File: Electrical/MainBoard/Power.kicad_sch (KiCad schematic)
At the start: 17 parts, among them J13 USB_B_Micro, J14 Battery1, J2 3.3V Supply, J3 5V Supply, SW1 5V Bypass, SW2 All Power Switch, U1 AP2114HA-3.3TRG1

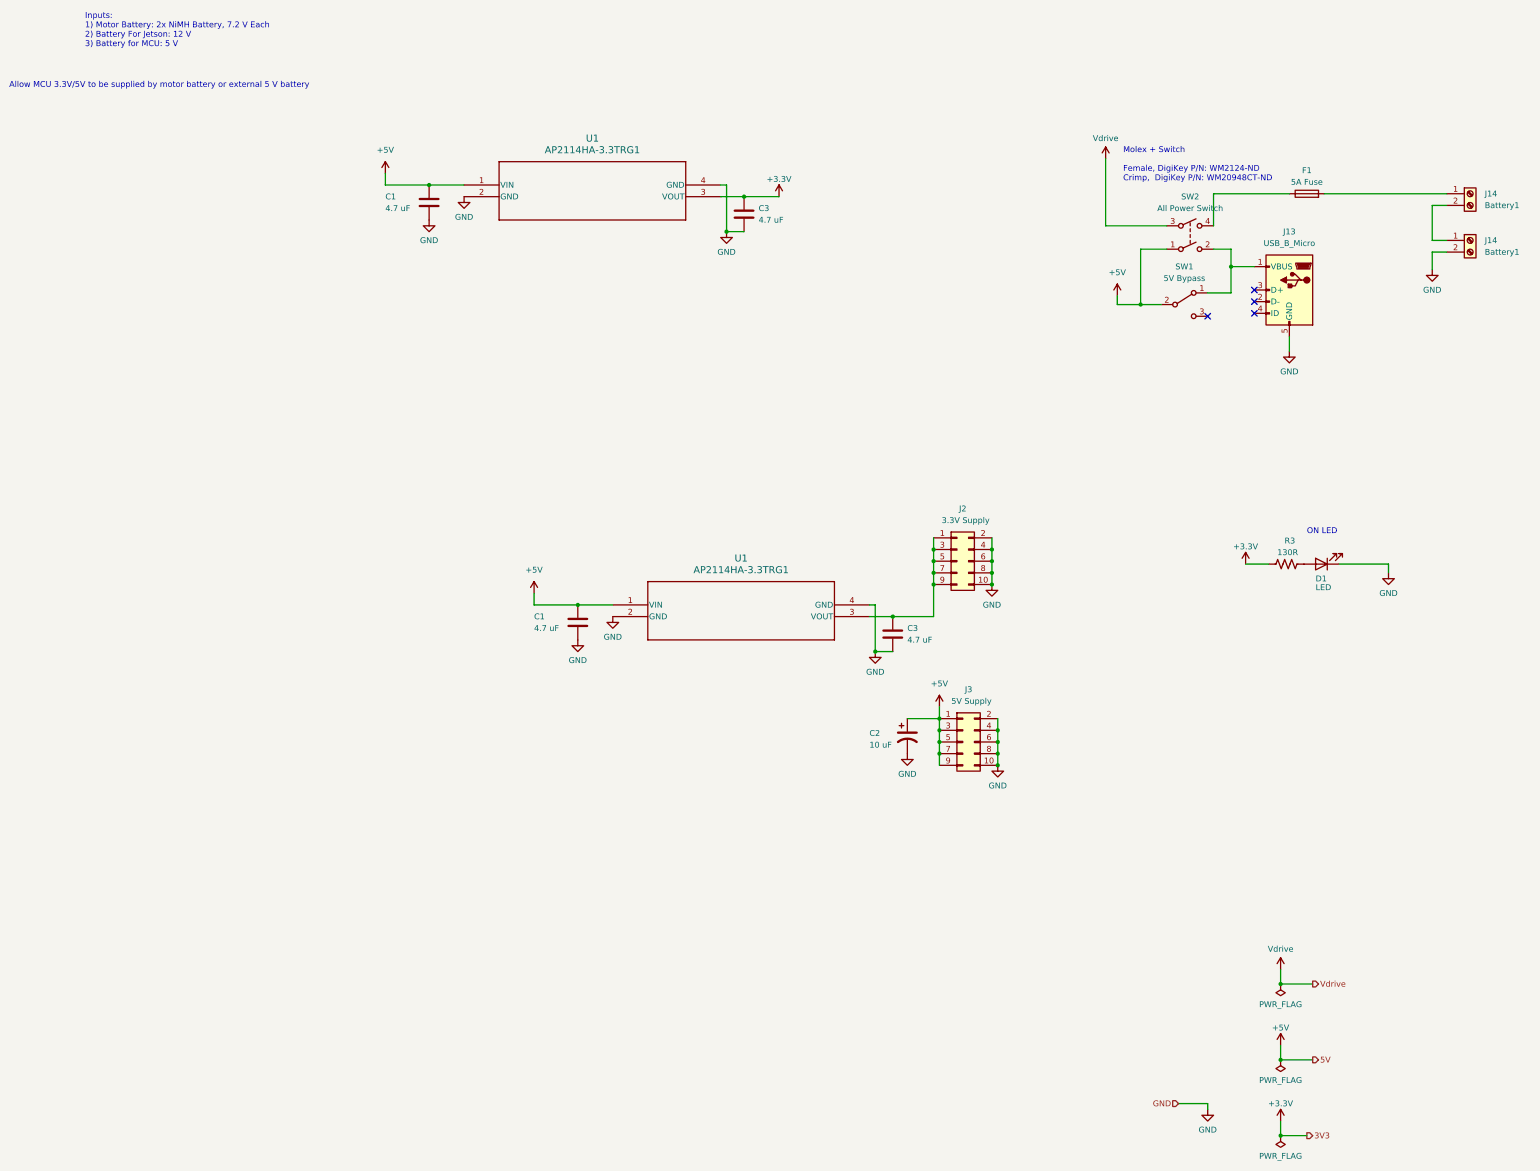
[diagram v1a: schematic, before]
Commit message: Fix SPI3 and make visual improvements
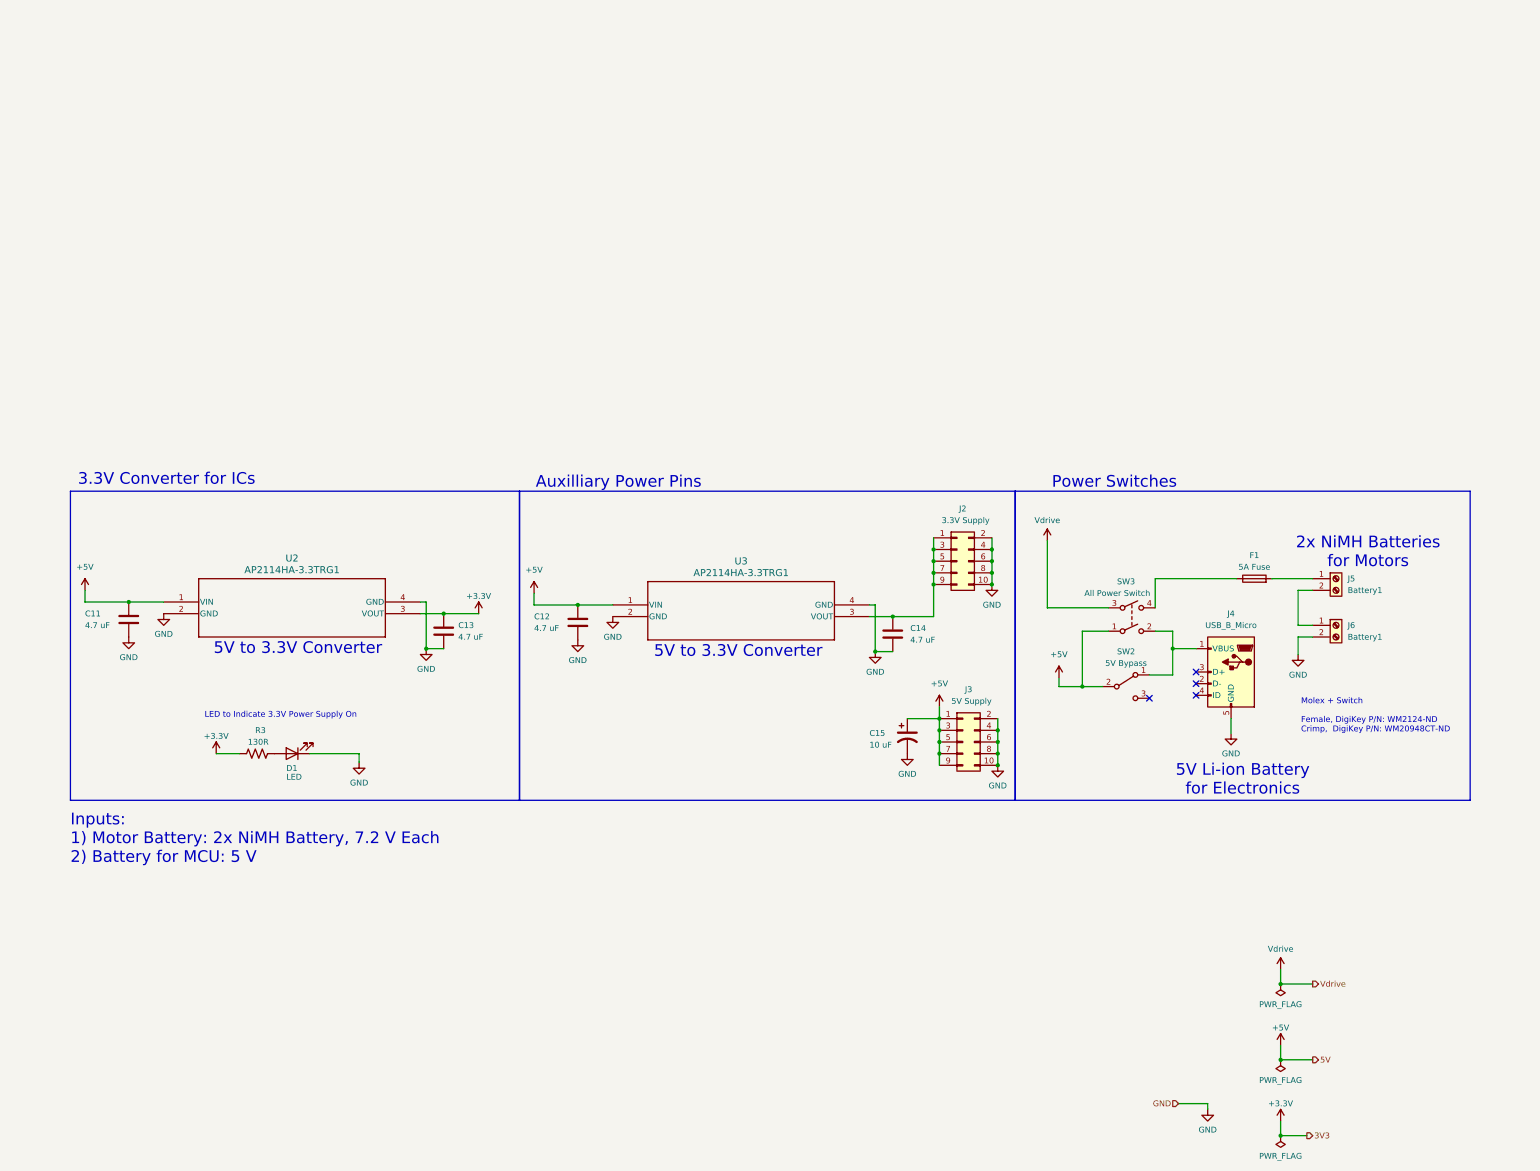
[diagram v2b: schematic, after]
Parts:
- renumbered C1 to C11, C1 to C12, C3 to C13, C3 to C14, C2 to C15, J13 to J4, J14 to J5, J14 to J6, SW1 to SW2, SW2 to SW3, U1 to U2, U1 to U3
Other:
- note added: "2x NiMH Batteries for Motors"
- note added: "3.3V Converter for ICs"
- note added: "5V Li-ion Battery for Electronics"
- note added: "5V to 3.3V Converter"
- note added: "Auxilliary Power Pins"
- note added: "Inputs: 1) Motor Battery: 2x NiMH Battery, 7.2 V Each 2) Battery for MCU: 5 V"
- note added: "LED to Indicate 3.3V Power Supply On"
- note added: "Power Switches"
- note removed: "Allow MCU 3.3V/5V to be supplied by motor battery or external 5 V battery"
- note removed: "Inputs: 1) Motor Battery: 2x NiMH Battery, 7.2 V Each 2) Battery For Jetson: 12 V 3) Battery for MCU: 5 V"
- note removed: "ON LED"
- moved on the sheet: C11, C13, D1, F1, J4, J5, J6, R3, SW2, SW3, U2

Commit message: Add updated gerbers
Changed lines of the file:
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@@
 	)
 	(junction
+		(at 269.24 254)
+		(diameter 0)
+		(color 0 0 0 0)
+	)
+	(junction
 		(at 285.115 260.985)
 		(diameter 0)
@@
 	(wire
 		(pts
-			(xy 34.29 144.78) (xy 24.765 144.78)
+			(xy 34.29 144.78) (xy 25.4 144.78)
 		)
 		(stroke
@@
 	(wire
 		(pts
-			(xy 84.455 177.8) (xy 84.455 179.705)
+			(xy 83.82 177.8) (xy 83.82 180.34)
 		)
 		(stroke
@@
 	(wire
 		(pts
-			(xy 73.66 177.8) (xy 84.455 177.8)
-		)
-		(stroke
-			(width 0)
-			(type default)
-		)
-	)
-	(wire
-		(pts
-			(xy 24.765 142.24) (xy 24.765 144.78)
+			(xy 73.66 177.8) (xy 83.82 177.8)
 		)
 		(stroke
@@
 	(symbol
 		(lib_id "power:GND")
-		(at 41.91 147.32 0)
-		(unit 1)
-		(exclude_from_sim no)
-		(in_bom yes)
-		(on_board yes)
-		(dnp no)
-		(fields_autoplaced yes)
-		(property "Reference" "#PWR0191"
-			(at 41.91 153.67 0)
-			(effects
-				(font
-					(size 1.27 1.27)
-				)
-				(hide yes)
-			)
-		)
-		(property "Value" "GND"
-			(at 41.91 151.765 0)
-			(effects
-				(font
-					(size 1.27 1.27)
-				)
-			)
-		)
-		(property "Footprint" ""
-			(at 41.91 147.32 0)
-			(effects
-				(font
-					(size 1.27 1.27)
-				)
-				(hide yes)
-			)
-		)
-		(property "Datasheet" ""
-			(at 41.91 147.32 0)
-			(effects
-				(font
-					(size 1.27 1.27)
-				)
-				(hide yes)
-			)
-		)
-		(property "Description" ""
-			(at 41.91 147.32 0)
-			(effects
-				(font
-					(size 1.27 1.27)
-				)
-			)
-		)
-		(pin "1"
-		)
-		(instances
-			(project "MainBoard"
-				(path "/bd24c4db-4e36-4117-bd4f-5228ef241da9/cf2778d1-0cc7-4750-89d4-9f2327b2ee05"
-					(reference "#PWR0191")
-					(unit 1)
-				)
-			)
-		)
-	)
-	(symbol
-		(lib_id "power:GND")
 		(at 203.835 177.8 0)
 		(unit 1)
@@
 	(symbol
 		(lib_id "power:+5V")
-		(at 24.765 142.24 0)
+		(at 25.4 144.78 0)
 		(unit 1)
 		(exclude_from_sim no)
@@
 		(fields_autoplaced yes)
 		(property "Reference" "#PWR0189"
-			(at 24.765 146.05 0)
+			(at 25.4 148.59 0)
 			(effects
 				(font
@@
 		)
 		(property "Value" "+5V"
-			(at 24.765 137.16 0)
+			(at 25.4 139.7 0)
 			(effects
 				(font
@@
 		)
 		(property "Footprint" ""
-			(at 24.765 142.24 0)
+			(at 25.4 144.78 0)
 			(effects
 				(font
@@
 		)
 		(property "Datasheet" ""
-			(at 24.765 142.24 0)
+			(at 25.4 144.78 0)
 			(effects
 				(font
@@
 		)
 		(property "Description" ""
-			(at 24.765 142.24 0)
+			(at 25.4 144.78 0)
 			(effects
 				(font
@@
 	(symbol
 		(lib_id "power:GND")
-		(at 84.455 179.705 0)
+		(at 83.82 180.34 0)
 		(unit 1)
 		(exclude_from_sim no)
@@
 		(fields_autoplaced yes)
 		(property "Reference" "#PWR0210"
-			(at 84.455 186.055 0)
+			(at 83.82 186.69 0)
 			(effects
 				(font
@@
 		)
 		(property "Value" "GND"
-			(at 84.455 184.15 0)
+			(at 83.82 184.785 0)
 			(effects
 				(font
@@
 		)
 		(property "Footprint" ""
-			(at 84.455 179.705 0)
+			(at 83.82 180.34 0)
 			(effects
 				(font
@@
 		)
 		(property "Datasheet" ""
-			(at 84.455 179.705 0)
+			(at 83.82 180.34 0)
 			(effects
 				(font
@@
 		)
 		(property "Description" ""
-			(at 84.455 179.705 0)
+			(at 83.82 180.34 0)
 			(effects
 				(font
@@
 	)
 	(symbol
+		(lib_id "power:GND")
+		(at 41.91 147.32 0)
+		(unit 1)
+		(exclude_from_sim no)
+		(in_bom yes)
+		(on_board yes)
+		(dnp no)
+		(fields_autoplaced yes)
+		(property "Reference" "#PWR046"
+			(at 41.91 153.67 0)
+			(effects
+				(font
+					(size 1.27 1.27)
+				)
+				(hide yes)
+			)
+		)
+		(property "Value" "GND"
+			(at 41.91 151.765 0)
+			(effects
+				(font
+					(size 1.27 1.27)
+				)
+			)
+		)
+		(property "Footprint" ""
+			(at 41.91 147.32 0)
+			(effects
+				(font
+					(size 1.27 1.27)
+				)
+				(hide yes)
+			)
+		)
+		(property "Datasheet" ""
+			(at 41.91 147.32 0)
+			(effects
+				(font
+					(size 1.27 1.27)
+				)
+				(hide yes)
+			)
+		)
+		(property "Description" ""
+			(at 41.91 147.32 0)
+			(effects
+				(font
+					(size 1.27 1.27)
+				)
+			)
+		)
+		(pin "1"
+		)
+		(instances
+			(project "MainBoard"
+				(path "/bd24c4db-4e36-4117-bd4f-5228ef241da9/cf2778d1-0cc7-4750-89d4-9f2327b2ee05"
+					(reference "#PWR046")
+					(unit 1)
+				)
+			)
+		)
+	)
+	(symbol
 		(lib_id "Matts_Library:AP2114HA-3.3TRG1")
 		(at 139.7 145.415 0)
@@
 					(unit 1)
 				)
+			)
+		)
+	)
+	(symbol
+		(lib_id "power:PWR_FLAG")
+		(at 269.24 254 0)
+		(unit 1)
+		(exclude_from_sim no)
+		(in_bom yes)
+		(on_board yes)
+		(dnp no)
+		(fields_autoplaced yes)
+		(property "Reference" "#FLG01"
+			(at 269.24 252.095 0)
+			(effects
+				(font
+					(size 1.27 1.27)
+				)
+				(hide yes)
+			)
+		)
+		(property "Value" "PWR_FLAG"
+			(at 269.24 248.92 0)
+			(effects
+				(font
+					(size 1.27 1.27)
+				)
+			)
+		)
+		(property "Footprint" ""
+			(at 269.24 254 0)
+			(effects
+				(font
+					(size 1.27 1.27)
+				)
+				(hide yes)
+			)
+		)
+		(property "Datasheet" "~"
+			(at 269.24 254 0)
+			(effects
+				(font
+					(size 1.27 1.27)
+				)
+				(hide yes)
+			)
+		)
+		(property "Description" "Special symbol for telling ERC where power comes from"
+			(at 269.24 254 0)
+			(effects
+				(font
+					(size 1.27 1.27)
+				)
+				(hide yes)
+			)
+		)
+		(pin "1"
+		)
+		(instances
+			(project ""
+				(path "/bd24c4db-4e36-4117-bd4f-5228ef241da9/cf2778d1-0cc7-4750-89d4-9f2327b2ee05"
+					(reference "#FLG01")
+					(unit 1)
+				)

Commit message: Update some parts
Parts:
- D1: Mfr Würth Elektronik -> Harvatek Corporation; Mfr P/N 150080RS75000 -> B1701URO-20D000114U1930; Supplier 1 P/N 732-4984-1-ND -> 3147-B1701URO-20D000114U1930CT-ND
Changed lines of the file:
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@@
 			)
 		)
-		(property "Datasheet" "https://www.we-online.com/katalog/datasheet/150080RS75000.pdf"
+		(property "Datasheet" "https://mm.digikey.com/Volume0/opasdata/d220001/medias/docus/3739/B1701URO-20D000114U1930.pdf"
 			(at 69.85 177.8 0)
 			(effects
@@
 			)
 		)
-		(property "Description" "LED RED CLEAR 0805 SMD"
+		(property "Description" "LED RED DIFFUSED 0805 SMD"
 			(at 69.85 177.8 0)
 			(effects
@@
 			)
 		)
-		(property "Mfr" "Würth Elektronik"
+		(property "Mfr" "Harvatek Corporation"
 			(at 69.85 177.8 0)
 			(effects
@@
 			)
 		)
-		(property "Mfr P/N" "150080RS75000"
+		(property "Mfr P/N" "B1701URO-20D000114U1930"
 			(at 69.85 177.8 0)
 			(effects
@@
 			)
 		)
-		(property "Supplier 1 P/N" "732-4984-1-ND"
+		(property "Supplier 1 P/N" "3147-B1701URO-20D000114U1930CT-ND"
 			(at 69.85 177.8 0)
 			(effects
